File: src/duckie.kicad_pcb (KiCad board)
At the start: 2 copper layers, 55.6 x 56.8 mm, 6 parts, among them SW1 SW_Push

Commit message: Updated PCB with buzz motor and potentiometer, and updated JOURNAL.md
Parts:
- added M1: Motor_DC, Connector_PinHeader_2.54mm:PinHeader_1x02_P2.54mm_Vertical, B.Cu at (183.2, 109.0)
- added RV1: R_Potentiometer, Potentiometer_THT:Potentiometer_Vishay_T73YP_Vertical, B.Cu at (208.1, 112.8)
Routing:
- net Net-(BT1--): track 30.3 -> 55.2 mm
- net Net-(R1-Pad1): track 44.4 -> 63.4 mm

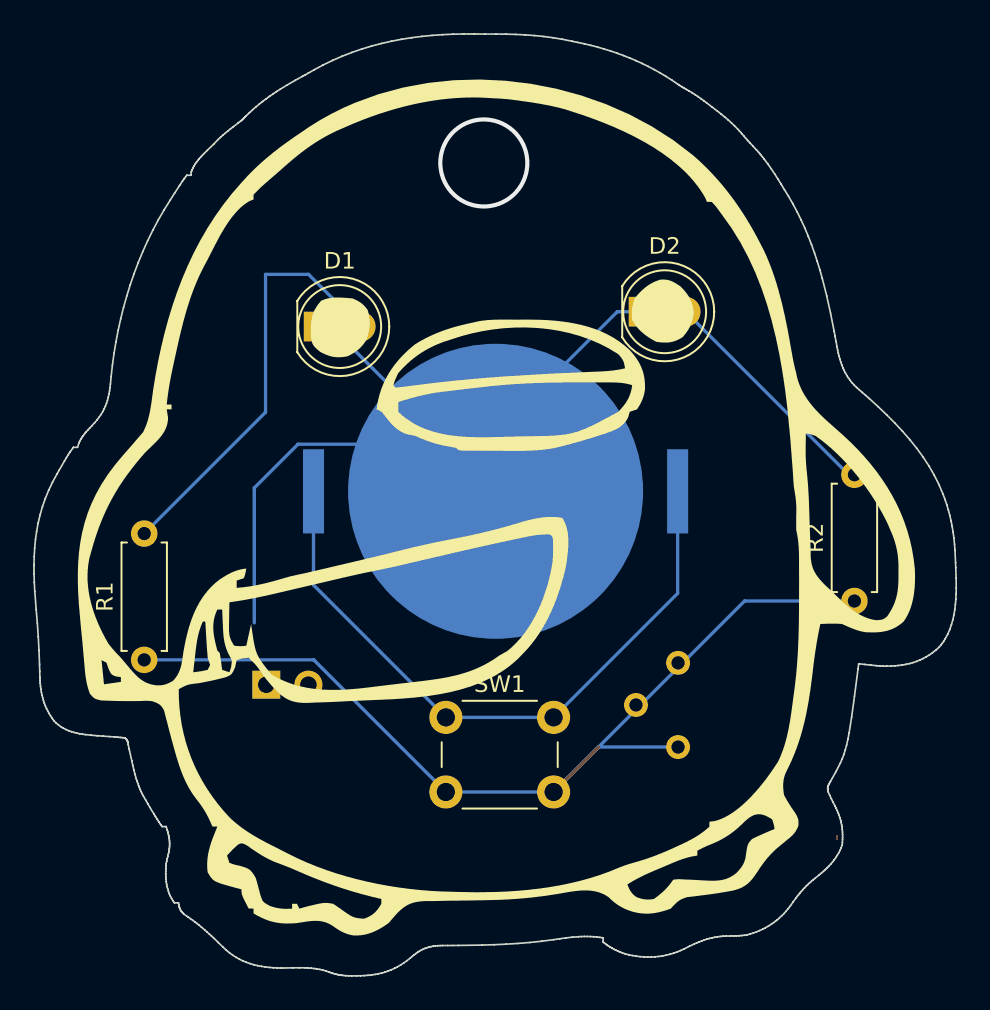
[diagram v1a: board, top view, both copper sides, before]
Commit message: Changing potentiometer wiring
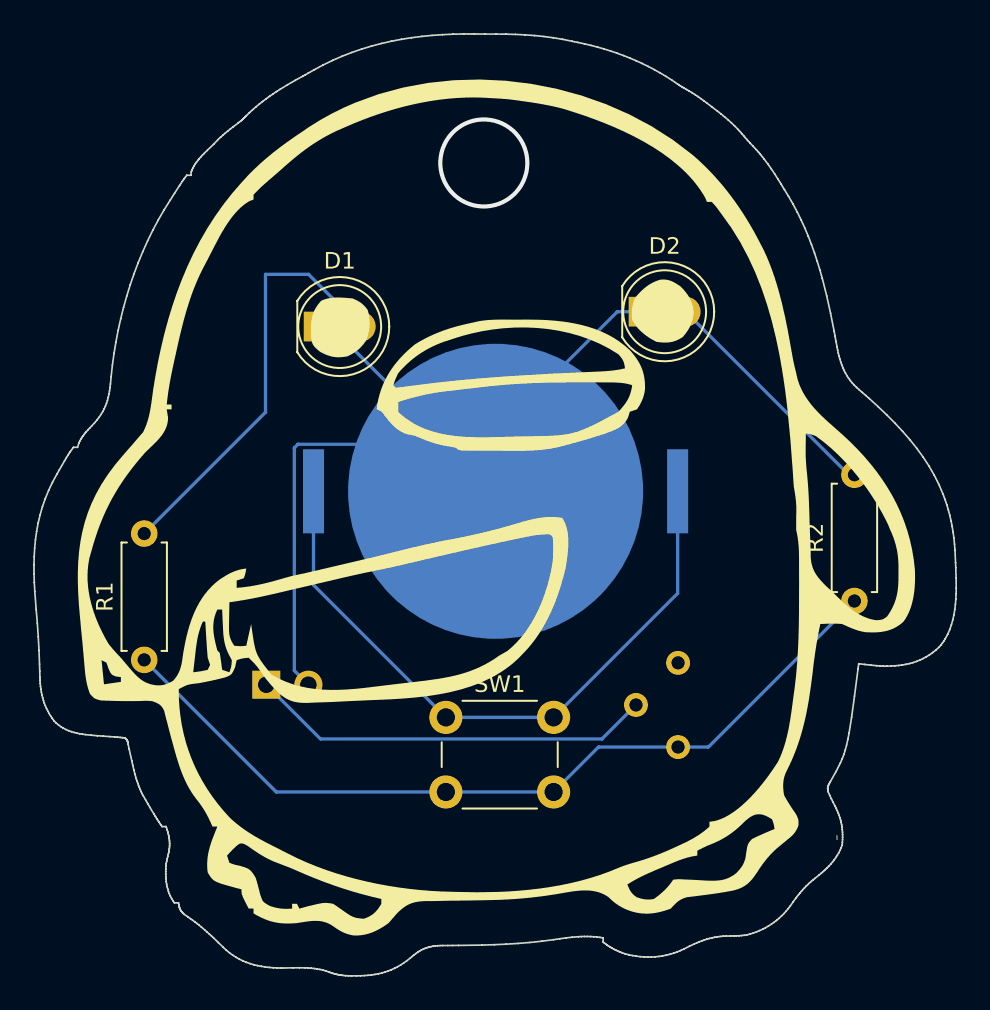
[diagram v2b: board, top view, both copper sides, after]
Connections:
- RV1 pad 2: unconnected-(RV1-Pad2) -> Net-(M1-+)
- RV1 pad 3: Net-(M1-+) -> unconnected-(RV1-Pad3)
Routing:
- net Net-(M1-+): track 0.00 -> 24.5 mm
- net Net-(R1-Pad1): track 63.4 -> 50.9 mm
- net Net-(BT1--): track 55.2 -> 58.3 mm
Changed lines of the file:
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@@
 	(net 5 "Net-(R1-Pad1)")
 	(net 6 "Net-(M1-+)")
-	(net 7 "unconnected-(RV1-Pad2)")
+	(net 7 "unconnected-(RV1-Pad3)")
 	(footprint "LED_THT:LED_D5.0mm"
 		(layer "F.Cu")
@@
 			(layers "*.Cu" "*.Mask")
 			(remove_unused_layers no)
-			(net 7 "unconnected-(RV1-Pad2)")
+			(net 6 "Net-(M1-+)")
 			(pinfunction "2")
 			(pintype "passive")
@@
 			(layers "*.Cu" "*.Mask")
 			(remove_unused_layers no)
-			(net 6 "Net-(M1-+)")
+			(net 7 "unconnected-(RV1-Pad3)")
 			(pinfunction "3")
 			(pintype "passive")
@@
 	)
 	(segment
-		(start 204.39459 86.52541)
-		(end 197.050103 93.869897)
+		(start 185.755 109.03)
+		(end 184.905 108.18)
 		(width 0.2)
 		(layer "B.Cu")
@@
 	)
 	(segment
-		(start 185.129103 94.519)
-		(end 182.49 97.158103)
+		(start 204.39459 86.52541)
+		(end 197.050103 93.869897)
 		(width 0.2)
 		(layer "B.Cu")
@@
 	)
 	(segment
-		(start 197.050103 97.36)
+		(start 185.129103 94.519)
 		(end 194.209103 94.519)
 		(width 0.2)
@@
 	)
 	(segment
-		(start 194.209103 94.519)
+		(start 184.905 108.18)
+		(end 184.905 94.743103)
+		(width 0.2)
+		(layer "B.Cu")
+		(net 1)
+	)
+	(segment
+		(start 184.905 94.743103)
 		(end 185.129103 94.519)
 		(width 0.2)
@@
 	)
 	(segment
-		(start 187.110103 87.42)
+		(start 194.209103 94.519)
 		(end 197.050103 97.36)
 		(width 0.2)
@@
 	)
 	(segment
-		(start 197.050103 93.869897)
+		(start 187.110103 87.42)
 		(end 197.050103 97.36)
 		(width 0.2)
@@
 	)
 	(segment
-		(start 182.49 97.158103)
-		(end 182.49 105.3)
+		(start 197.050103 93.869897)
+		(end 197.050103 97.36)
 		(width 0.2)
 		(layer "B.Cu")
@@
 	)
 	(segment
+		(start 183.82 115.5)
+		(end 175.85 107.53)
+		(width 0.2)
+		(layer "B.Cu")
+		(net 5)
+	)
+	(segment
 		(start 203.26 112.79)
-		(end 200.55 115.5)
+		(end 208.06 112.79)
 		(width 0.2)
-		(layer "F.Cu")
+		(layer "B.Cu")
 		(net 5)
 	)
 	(segment
 		(start 200.55 115.5)
-		(end 212.07 103.98)
+		(end 203.26 112.79)
 		(width 0.2)
 		(layer "B.Cu")
@@
 	)
 	(segment
-		(start 194.05 115.5)
-		(end 186.08 107.53)
+		(start 208.06 112.79)
+		(end 209.89 112.79)
 		(width 0.2)
 		(layer "B.Cu")
@@
 	)
 	(segment
-		(start 203.26 112.79)
-		(end 208.06 112.79)
+		(start 194.05 115.5)
+		(end 183.82 115.5)
 		(width 0.2)
 		(layer "B.Cu")
@@
 	)
 	(segment
-		(start 200.55 115.5)
-		(end 203.26 112.79)
+		(start 209.89 112.79)
+		(end 218.7 103.98)
 		(width 0.2)
 		(layer "B.Cu")
@@
 	)
 	(segment
-		(start 186.08 107.53)
-		(end 175.85 107.53)
+		(start 203.469 112.301)
+		(end 205.52 110.25)
 		(width 0.2)
 		(layer "B.Cu")
-		(net 5)
+		(net 6)
 	)
 	(segment
-		(start 212.07 103.98)
-		(end 218.7 103.98)
+		(start 183.215 109.03)
+		(end 186.486 112.301)
 		(width 0.2)
 		(layer "B.Cu")
-		(net 5)
+		(net 6)
+	)
+	(segment
+		(start 186.486 112.301)
+		(end 203.469 112.301)
+		(width 0.2)
+		(layer "B.Cu")
+		(net 6)
 	)
 	(group ""
